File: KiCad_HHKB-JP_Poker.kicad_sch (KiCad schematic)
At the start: 21 parts, among them SW1 SW_Push, U1 ATmega32U4-MU, U2 PRTR5V0U2X, Y1 16MHz

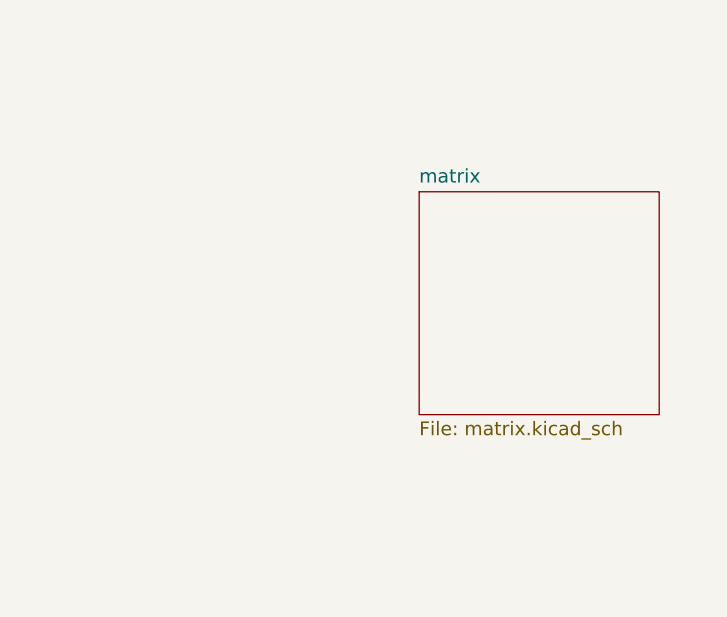
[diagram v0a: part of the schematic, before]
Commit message: Edit Key Matrix
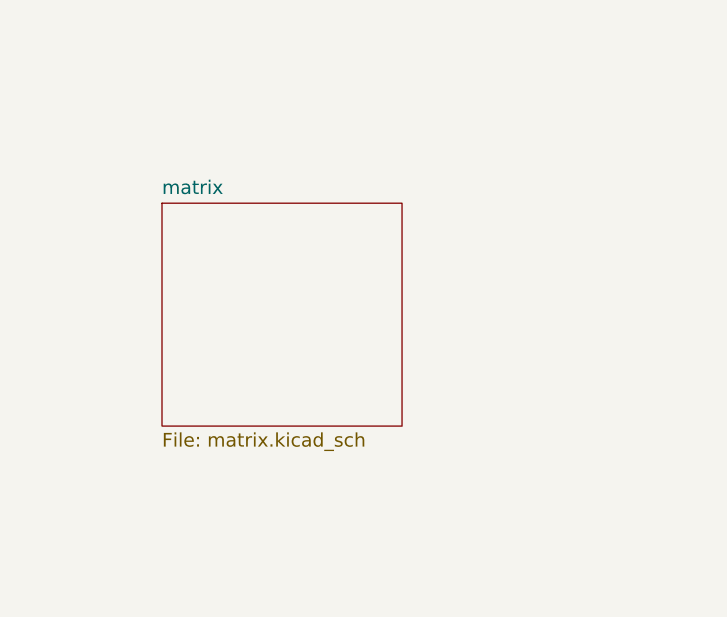
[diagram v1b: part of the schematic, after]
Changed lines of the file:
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@@
     (pin "1")
   )
-  (sheet (at 215.9 108.585) (size 26.67 24.765) (fields_autoplaced)
+  (sheet (at 187.325 109.855) (size 26.67 24.765) (fields_autoplaced)
     (stroke (width 0) (type solid) (color 0 0 0 0))
     (fill (color 0 0 0 0.0000))
-    (property "Sheet name" "matrix" (id 0) (at 215.9 107.7464 0)
+    (property "Sheet name" "matrix" (id 0) (at 187.325 109.0164 0)
       (effects (font (size 1.524 1.524)) (justify left bottom))
     )
-    (property "Sheet file" "matrix.kicad_sch" (id 1) (at 215.9 134.0362 0)
+    (property "Sheet file" "matrix.kicad_sch" (id 1) (at 187.325 135.3062 0)
       (effects (font (size 1.524 1.524)) (justify left top))
     )
@@
       (reference "D9") (unit 1) (value "SOD-123") (footprint "Diode_SMD:D_SOD-123")
     )
-    (path "/00000000-0000-0000-0000-00005a286589/00000000-0000-0000-0000-000060eead43"
+    (path "/00000000-0000-0000-0000-00005a286589/c5212977-2a89-457f-9cd7-ff57379b72b3"
       (reference "D10") (unit 1) (value "SOD-123") (footprint "Diode_SMD:D_SOD-123")
     )
-    (path "/00000000-0000-0000-0000-00005a286589/00000000-0000-0000-0000-00005faa46ad"
+    (path "/00000000-0000-0000-0000-00005a286589/636e8c86-311a-4d32-9d49-68188313c166"
       (reference "D11") (unit 1) (value "SOD-123") (footprint "Diode_SMD:D_SOD-123")
     )
@@
       (reference "D36") (unit 1) (value "SOD-123") (footprint "Diode_SMD:D_SOD-123")
     )
+    (path "/00000000-0000-0000-0000-00005a286589/c4f8b622-036c-4c4e-a477-44a007332937"
+      (reference "D37") (unit 1) (value "SOD-123") (footprint "Diode_SMD:D_SOD-123")
+    )
     (path "/00000000-0000-0000-0000-00005a286589/00000000-0000-0000-0000-00005d45f5be"
       (reference "D38") (unit 1) (value "SOD-123") (footprint "Diode_SMD:D_SOD-123")
@@
       (reference "D41") (unit 1) (value "SOD-123") (footprint "Diode_SMD:D_SOD-123")
     )
-    (path "/00000000-0000-0000-0000-00005a286589/00000000-0000-0000-0000-00005d497cb8"
+    (path "/00000000-0000-0000-0000-00005a286589/681f0acc-74d9-4353-b7dd-8e246d77ba91"
       (reference "D42") (unit 1) (value "SOD-123") (footprint "Diode_SMD:D_SOD-123")
+    )
+    (path "/00000000-0000-0000-0000-00005a286589/65525a24-577a-4454-8197-3f3f2409802c"
+      (reference "D43") (unit 1) (value "SOD-123") (footprint "Diode_SMD:D_SOD-123")
     )
     (path "/00000000-0000-0000-0000-00005a286589/00000000-0000-0000-0000-00005d45f5cb"
@@
       (reference "K_H1") (unit 1) (value "MX-NoLED") (footprint "MX_Only:MXOnly-1U-Hotswap")
     )
+    (path "/00000000-0000-0000-0000-00005a286589/d3ebf770-4bd2-467a-989e-abeefc1a0471"
+      (reference "K_HENK1") (unit 1) (value "MX-NoLED") (footprint "MX_Only:MXOnly-1U-Hotswap")
+    )
     (path "/00000000-0000-0000-0000-00005a286589/00000000-0000-0000-0000-00005d47fe7e"
       (reference "K_I1") (unit 1) (value "MX-NoLED") (footprint "MX_Only:MXOnly-1U-Hotswap")
@@
       (reference "K_LCTRL1") (unit 1) (value "MX-NoLED") (footprint "MX_Only:MXOnly-1.25U-Hotswap")
     )
-    (path "/00000000-0000-0000-0000-00005a286589/00000000-0000-0000-0000-00005faa46a7"
-      (reference "K_LGUI1") (unit 1) (value "MX-NoLED") (footprint "MX_Only:MXOnly-1U-Hotswap")
-    )
     (path "/00000000-0000-0000-0000-00005a286589/00000000-0000-0000-0000-00005d497b7a"
       (reference "K_LSFT1") (unit 1) (value "MX-NoLED") (footprint "MX_Only:MXOnly-2.25U-Hotswap")
     )
+    (path "/00000000-0000-0000-0000-00005a286589/1ef0d427-de6f-4a84-9a45-e41f4820a2ef"
+      (reference "K_LSPACE1") (unit 1) (value "MX-NoLED") (footprint "MX_Only:MXOnly-1.25U-Hotswap")
+    )
     (path "/00000000-0000-0000-0000-00005a286589/00000000-0000-0000-0000-00005d497be2"
       (reference "K_M1") (unit 1) (value "MX-NoLED") (footprint "MX_Only:MXOnly-1U-Hotswap")
@@
     )
     (path "/00000000-0000-0000-0000-00005a286589/00000000-0000-0000-0000-000060ee8a21"
-      (reference "K_NFER1") (unit 1) (value "MX-NoLED") (footprint "MX_Only:MXOnly-1.25U-Hotswap")
+      (reference "K_NHENK1") (unit 1) (value "MX-NoLED") (footprint "MX_Only:MXOnly-1.25U-Hotswap")
     )
     (path "/00000000-0000-0000-0000-00005a286589/00000000-0000-0000-0000-00005d47fe8b"
@@
       (reference "K_RGUI1") (unit 1) (value "MX-NoLED") (footprint "MX_Only:MXOnly-1U-Hotswap")
     )
+    (path "/00000000-0000-0000-0000-00005a286589/159bf2bd-c3fa-4f3a-b40f-5928930f486e"
+      (reference "K_RSPACE1") (unit 1) (value "MX-NoLED") (footprint "MX_Only:MXOnly-1.25U-Hotswap")
+    )
     (path "/00000000-0000-0000-0000-00005a286589/00000000-0000-0000-0000-00005d47ff0d"
       (reference "K_S1") (unit 1) (value "MX-NoLED") (footprint "MX_Only:MXOnly-1U-Hotswap")
@@
       (reference "K_SBSPC2") (unit 1) (value "MX-NoLED") (footprint "MX_Only:MXOnly-1U-Hotswap")
     )
-    (path "/00000000-0000-0000-0000-00005a286589/00000000-0000-0000-0000-00005d497cb2"
-      (reference "K_SPC1") (unit 1) (value "MX-NoLED") (footprint "MX_Only:MXOnly-6U-Centered-Hotswap-ReversedStabilizers")
-    )
-    (path "/00000000-0000-0000-0000-00005a286589/00000000-0000-0000-0000-000060f7c6e2"
-      (reference "K_SPC2") (unit 1) (value "MX-NoLED") (footprint "MX_Only:MXOnly-1U-Hotswap")
-    )
     (path "/00000000-0000-0000-0000-00005a286589/00000000-0000-0000-0000-00005fb7e4d3"
       (reference "K_SRSFT1") (unit 1) (value "MX-NoLED") (footprint "MX_Only:MXOnly-1U-Hotswap")
@@
       (reference "K_U1") (unit 1) (value "MX-NoLED") (footprint "MX_Only:MXOnly-1U-Hotswap")
     )
+    (path "/00000000-0000-0000-0000-00005a286589/2509ecc1-7b87-4597-b2e5-0d72327a0dc3"
+      (reference "K_UpArr1") (unit 1) (value "MX-NoLED") (footprint "MX_Only:MXOnly-1U-Hotswap")
+    )
     (path "/00000000-0000-0000-0000-00005a286589/00000000-0000-0000-0000-00005d497bbb"
       (reference "K_V1") (unit 1) (value "MX-NoLED") (footprint "MX_Only:MXOnly-1U-Hotswap")
@@
       (reference "K_W1") (unit 1) (value "MX-NoLED") (footprint "MX_Only:MXOnly-1U-Hotswap")
     )
+    (path "/00000000-0000-0000-0000-00005a286589/2ffb9f99-9170-4eb4-9f63-3cbdacafa95b"
+      (reference "K_WIN1") (unit 1) (value "MX-NoLED") (footprint "MX_Only:MXOnly-1U-Hotswap")
+    )
     (path "/00000000-0000-0000-0000-00005a286589/00000000-0000-0000-0000-00005d497ba1"
       (reference "K_X1") (unit 1) (value "MX-NoLED") (footprint "MX_Only:MXOnly-1U-Hotswap")
     )
-    (path "/00000000-0000-0000-0000-00005a286589/00000000-0000-0000-0000-000060eead3d"
-      (reference "K_XFER1") (unit 1) (value "MX-NoLED") (footprint "MX_Only:MXOnly-1.25U-Hotswap")
-    )
     (path "/00000000-0000-0000-0000-00005a286589/00000000-0000-0000-0000-00005d47fe64"
